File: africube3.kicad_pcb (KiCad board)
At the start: 4 copper layers, 66.5 x 89.5 mm, 41 parts, among them IC1 ADC-20-4, J1 SMA Edge FM, J2 Conn_01x04, J3 RPi_GPIO, J4 Conn_01x02, U1 TQP7M9105, U2 SXBP-150+, U3 BA178M05FP-E2, U4 MCP3421A0T-E/CH

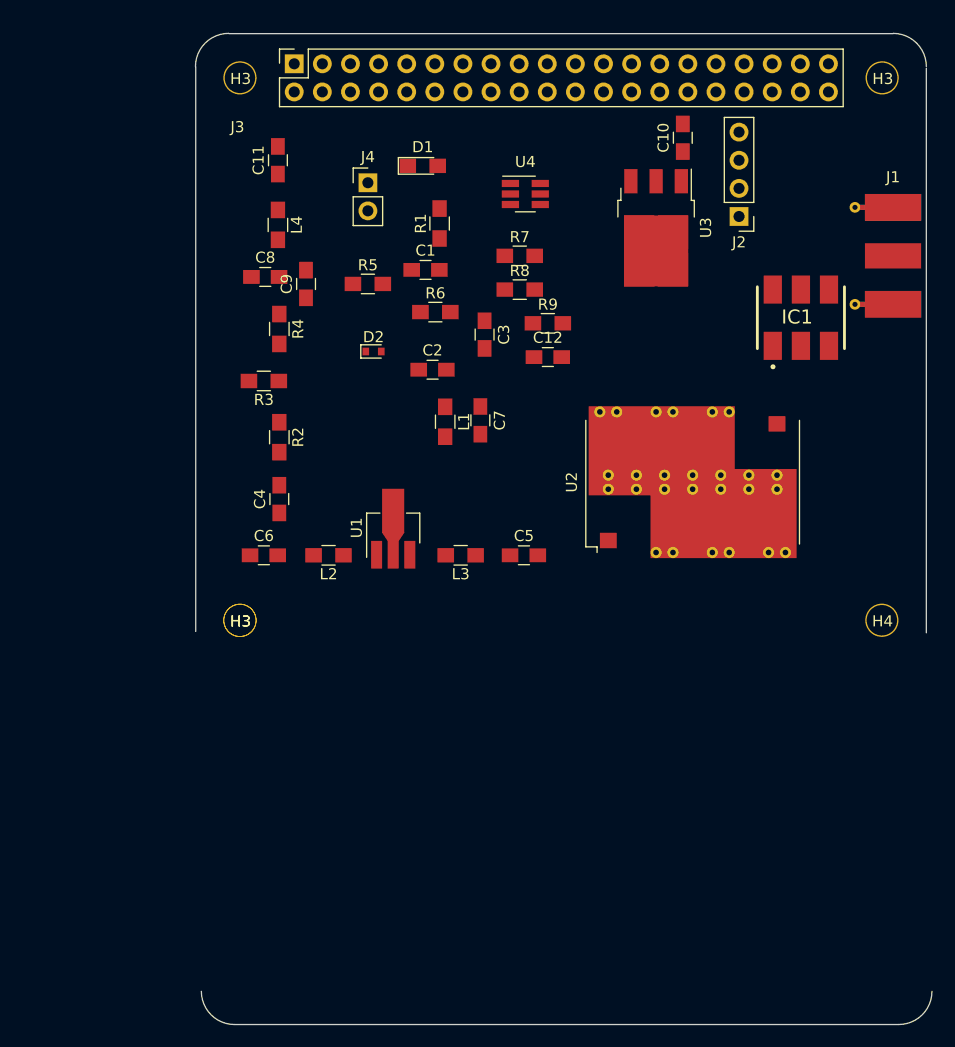
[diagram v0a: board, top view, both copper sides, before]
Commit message: removing power detector
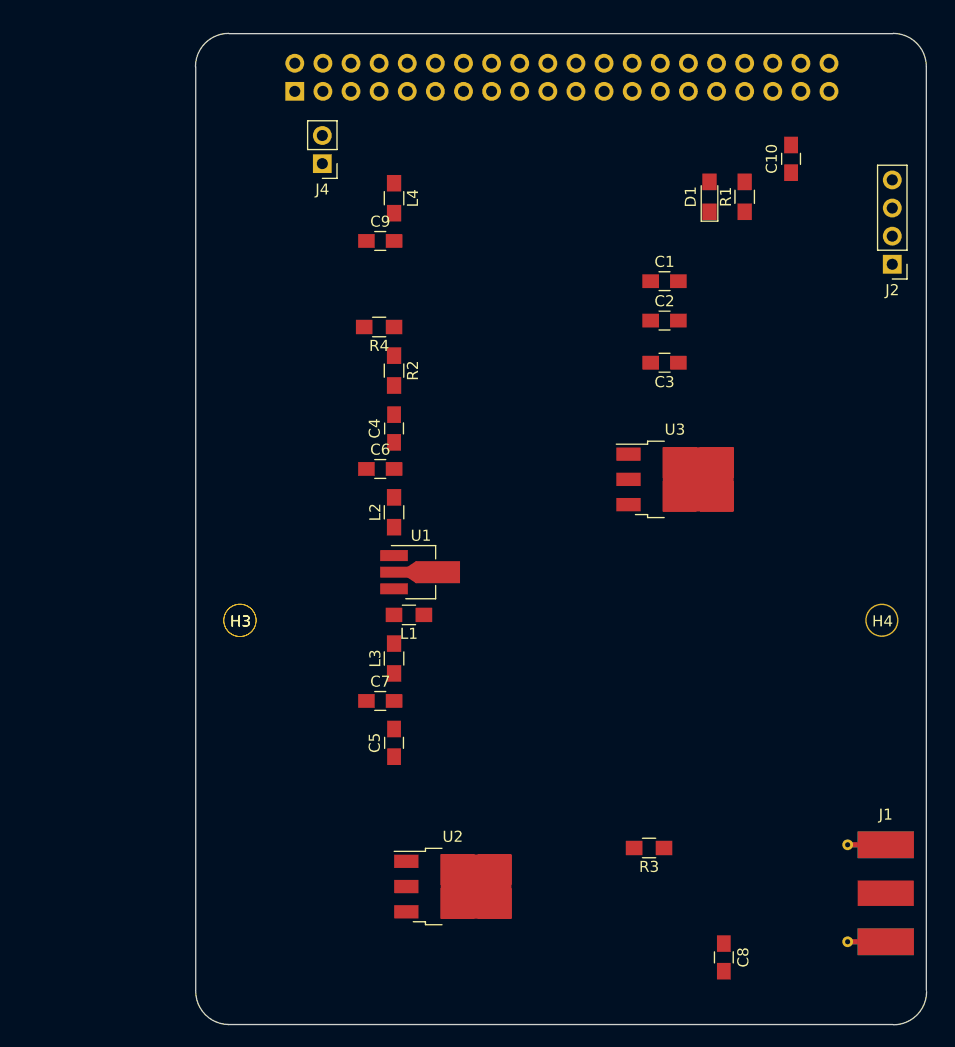
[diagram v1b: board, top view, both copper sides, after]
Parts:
- removed C11: 100pF, Capacitors_SMD:C_0805_HandSoldering
- removed C12: 1nF, Capacitors_SMD:C_0805_HandSoldering
- removed D2: SMS3922-079LF, Diodes_SMD:D_SOD-523
- removed the H3 at (139.0, 64.3)
- removed the H3 at (81.0, 64.3)
- removed IC1: ADC-20-4, rf_noise:ADC-20-4+
- removed R5: 0, Resistors_SMD:R_0805_HandSoldering
- removed R6, R7, R8, R9: 220K, Resistors_SMD:R_0805_HandSoldering
- removed U4: MCP3421A0T-E/CH, TO_SOT_Packages_SMD:SOT-23-6_Handsoldering
- C10: value 4.7uF 16V -> 100pF
- C8: value 100pF -> 10pF
- C9: value 10pF -> 4.7uF 16V
- J3: moved to B.Cu
- R3: value 50 -> OC
- R4: value OC -> 0
- U2: footprint RF_Mini-Circuits:Mini-Circuits_HF1139_LandPatternPL-230 -> TO_SOT_Packages_SMD:TO-252-3_TabPin4
- U3: footprint TO_SOT_Packages_SMD:TO-252-3_TabPin2 -> TO_SOT_Packages_SMD:TO-252-3_TabPin4
- moved C8 74.1 mm to (124.7, 143.8), turned to 270 degrees
- moved J1 57.6 mm to (137.6, 138.0)
- moved R3 54.7 mm to (118.0, 133.9)
- moved U2 42.5 mm to (100.3, 137.4), turned to 0 degrees
- moved R1 27.7 mm to (126.6, 75.1)
- moved C7 26.9 mm to (93.7, 120.6), turned to 0 degrees
- moved D1 26.1 mm to (123.4, 75.1), turned to 90 degrees
- moved U3 22.8 mm to (120.3, 100.6), turned to 0 degrees
- moved C1 21.6 mm to (119.4, 82.7)
- moved C2 21.4 mm to (119.4, 86.2)
- moved C5 20.6 mm to (94.9, 124.4), turned to 90 degrees
- moved L1 17.8 mm to (96.3, 112.8), turned to 180 degrees
- moved C3 16.5 mm to (119.4, 90.0), turned to 180 degrees
- moved J2 14.5 mm to (140.0, 81.2)
- moved C6 13.1 mm to (93.7, 99.6)
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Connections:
- C10 pad 2: GND -> Net-(C10-Pad2)
- C8 pad 1: Net-(C8-Pad1) -> GND
- C9 pad 1: GND -> Net-(C9-Pad1)
- C9 pad 2: Net-(C9-Pad2) -> GND
- J1 pad 1: Net-(IC1-Pad6) -> (no net)
- J2 pad 2: Net-(C10-Pad1) -> Net-(C9-Pad1)
- J3 pad 3: SDA -> (no net)
- J3 pad 5: SCL -> (no net)
- J3 pad 7: Net-(C11-Pad2) -> Net-(C10-Pad2)
- L4 pad 1: Net-(C11-Pad1) -> Net-(C10-Pad1)
- L4 pad 2: Net-(C9-Pad2) -> Net-(C8-Pad2)
- R3 pad 1: Net-(IC1-Pad4) -> Net-(R2-Pad1)
- R4 pad 1: Net-(R2-Pad1) -> Net-(C8-Pad2)
- R4 pad 2: GND -> Net-(R2-Pad1)
- U3 pad 1: Net-(C10-Pad1) -> Net-(C9-Pad1)
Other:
- board size 66.5 x 89.5 mm -> 66.1 x 89.6 mm

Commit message: removed power detection
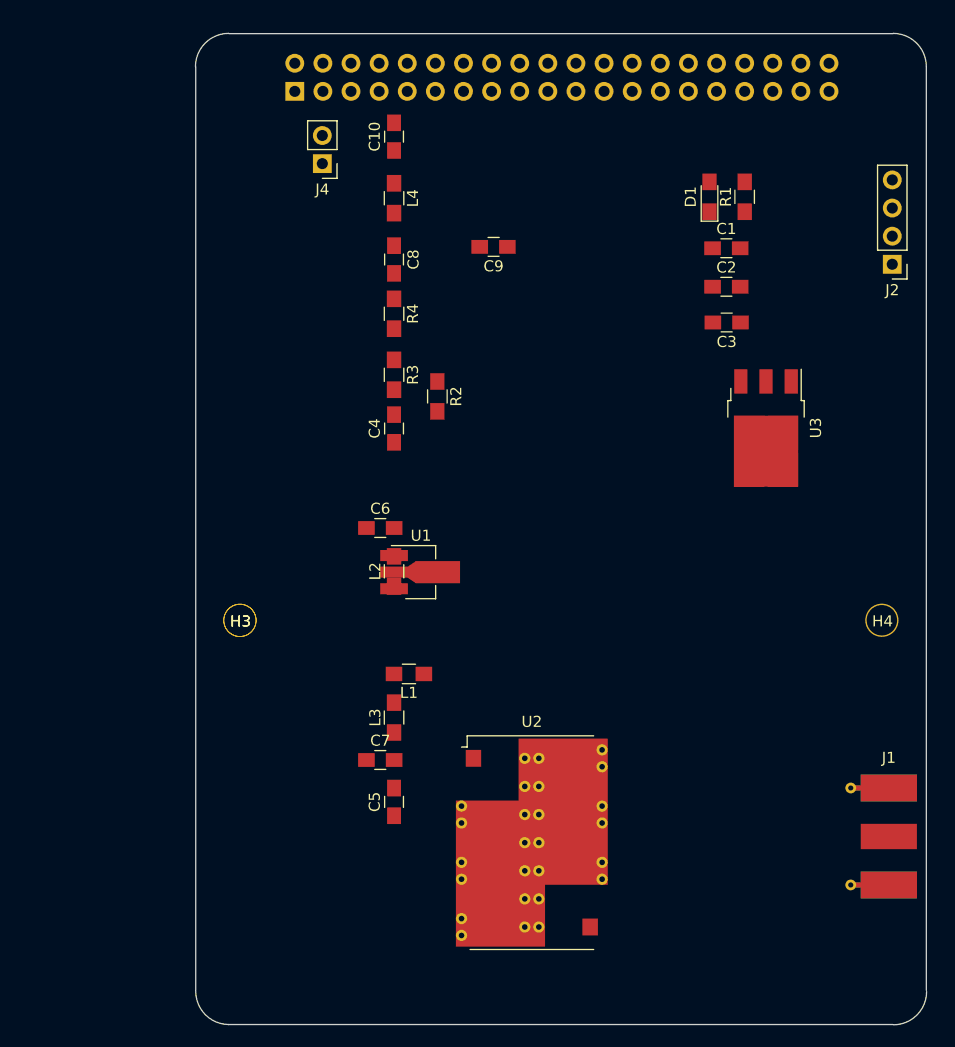
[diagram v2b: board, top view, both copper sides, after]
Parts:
- U2: footprint TO_SOT_Packages_SMD:TO-252-3_TabPin4 -> mini_filter:Mini-Circuits_HF1139_LandPatternPL-230
- moved C8 69.7 mm to (94.9, 80.7)
- moved R3 48.6 mm to (94.9, 91.1), turned to 270 degrees
- moved C10 35.9 mm to (94.9, 69.6)
- moved C9 10.3 mm to (103.9, 79.6), turned to 180 degrees
- moved U3 9.45 mm to (128.5, 95.9), turned to 270 degrees
- moved U2 8.16 mm to (107.4, 133.4)
- moved C3 6.69 mm to (125.0, 86.4)
- moved C2 6.37 mm to (125.0, 83.2)
- moved C1 6.33 mm to (125.0, 79.7)
- moved C5 5.33 mm to (94.9, 129.7)
- moved C6 5.33 mm to (93.7, 105.0)
- moved C7 5.33 mm to (93.7, 125.9)
- moved L3 5.33 mm to (94.9, 122.1)
- moved L1 5.33 mm to (96.3, 118.2)
- moved L2 5.33 mm to (94.9, 108.9)
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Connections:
- J1 pad 1: (no net) -> Net-(J1-Pad1)

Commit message: layout done need to do groundplanes
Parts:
- added H3: 3mm_Mounting_Hole, project_footprints:NPTH_3mm_ID, F.Cu at (81.0, 64.3)
- added H3 (x2): 3mm_Mounting_Hole, project_footprints:NPTH_3mm_ID, F.Cu at (81.6, 114.4)
- added H4: 3mm_Mounting_Hole, project_footprints:NPTH_3mm_ID, F.Cu at (139.0, 64.3)
- added H4: 3mm_Mounting_Hole, project_footprints:NPTH_3mm_ID, F.Cu at (139.0, 113.3)
- moved J4 37.9 mm to (126.3, 70.3), turned to 270 degrees
- moved C9 30.8 mm to (134.7, 79.9), turned to 270 degrees
- moved U2 10.2 mm to (116.3, 138.4), turned to 90 degrees
- moved C5 7.47 mm to (94.9, 137.2)
- moved U1 6.53 mm to (96.9, 115.5)
- moved C7 6.42 mm to (96.2, 131.9), turned to 180 degrees
- moved L3 4.42 mm to (94.9, 126.5)
- moved R2 3.93 mm to (94.9, 93.4)
- moved C4 3.53 mm to (94.9, 99.5)
- moved L1 2.92 mm to (96.3, 121.1)
- moved R3 2.81 mm to (96.3, 88.7), turned to 0 degrees
- moved C6 2.67 mm to (96.2, 104.0), turned to 180 degrees
- moved C8 1.67 mm to (96.2, 79.6), turned to 180 degrees
- moved R4 1.57 mm to (94.9, 84.0)
- moved H3 1.23 mm to (81.6, 114.4)
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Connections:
- J2 pad 4: Net-(J2-Pad4) -> GND
- J3 pad 1: Net-(J2-Pad4) -> (no net)
- J3 pad 17: Net-(J2-Pad4) -> (no net)
- U3 pad 2: (no net) -> GND
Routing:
- net GND: track 0.00 -> 312.9 mm, vias 0 -> 2
- net +5V: track 0.00 -> 92.9 mm
- net Net-(J3-Pad2): track 0.00 -> 70.9 mm
- net Net-(C9-Pad1): track 0.00 -> 20.7 mm
- net Net-(J1-Pad1): track 0.00 -> 16.3 mm
- net Net-(C5-Pad1): track 0.00 -> 16.2 mm
- net Net-(L1-Pad2): track 0.00 -> 8.18 mm
- net Net-(C5-Pad2): track 0.00 -> 8.07 mm
- net Net-(C4-Pad1): track 0.00 -> 6.70 mm
- net Net-(R2-Pad1): track 0.00 -> 6.68 mm
- net Net-(C8-Pad2): track 0.00 -> 6.19 mm
- net Net-(L2-Pad1): track 0.00 -> 3.84 mm
- net Net-(C4-Pad2): track 0.00 -> 3.50 mm
- net Net-(C10-Pad2): track 0.00 -> 3.40 mm
- net Net-(C10-Pad1): track 0.00 -> 2.96 mm
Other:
- copper layers 4 -> 2
- net class 5V2A added: clearance 0.4, trace_width 0.8, via_dia 0.4, via_drill 0.2
- net class Transmition_Line added: clearance 0.2, trace_width 1.05758, via_dia 3, via_drill 1.5

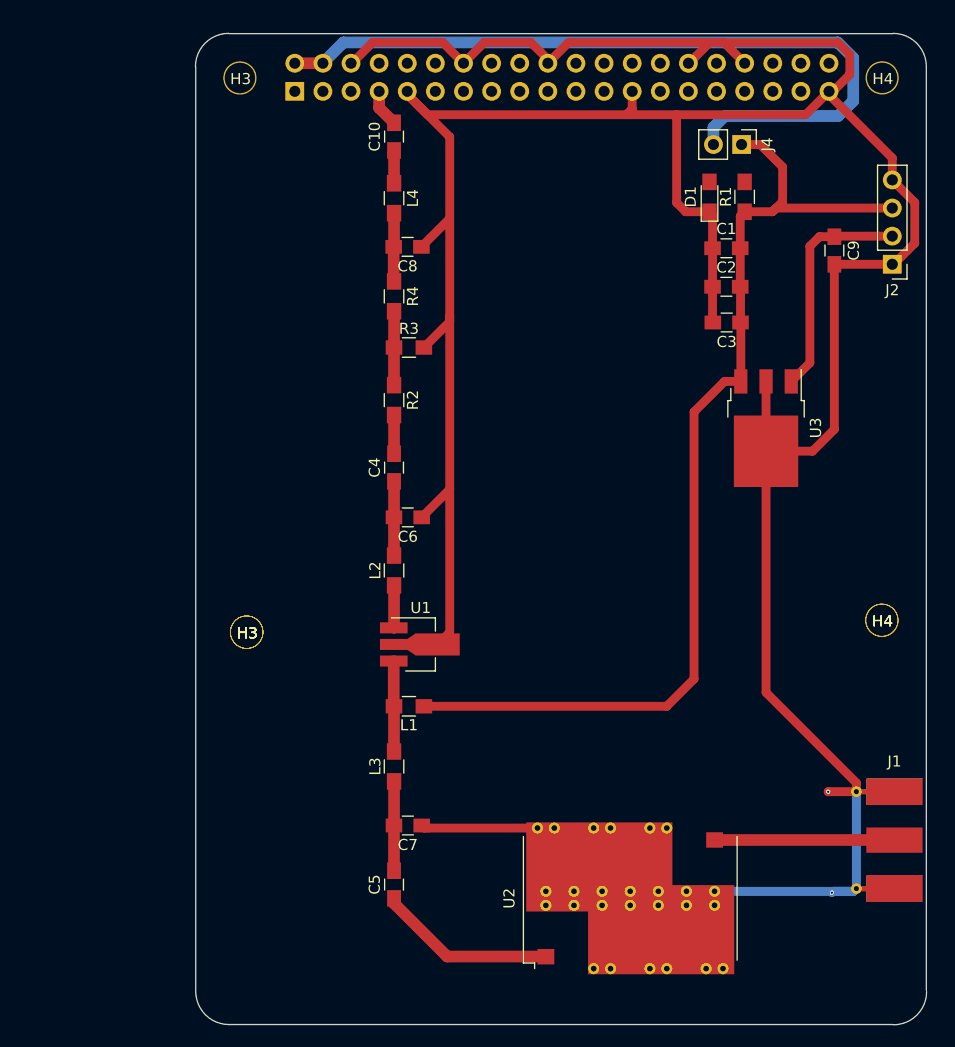
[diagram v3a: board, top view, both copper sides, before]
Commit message: added groundplane
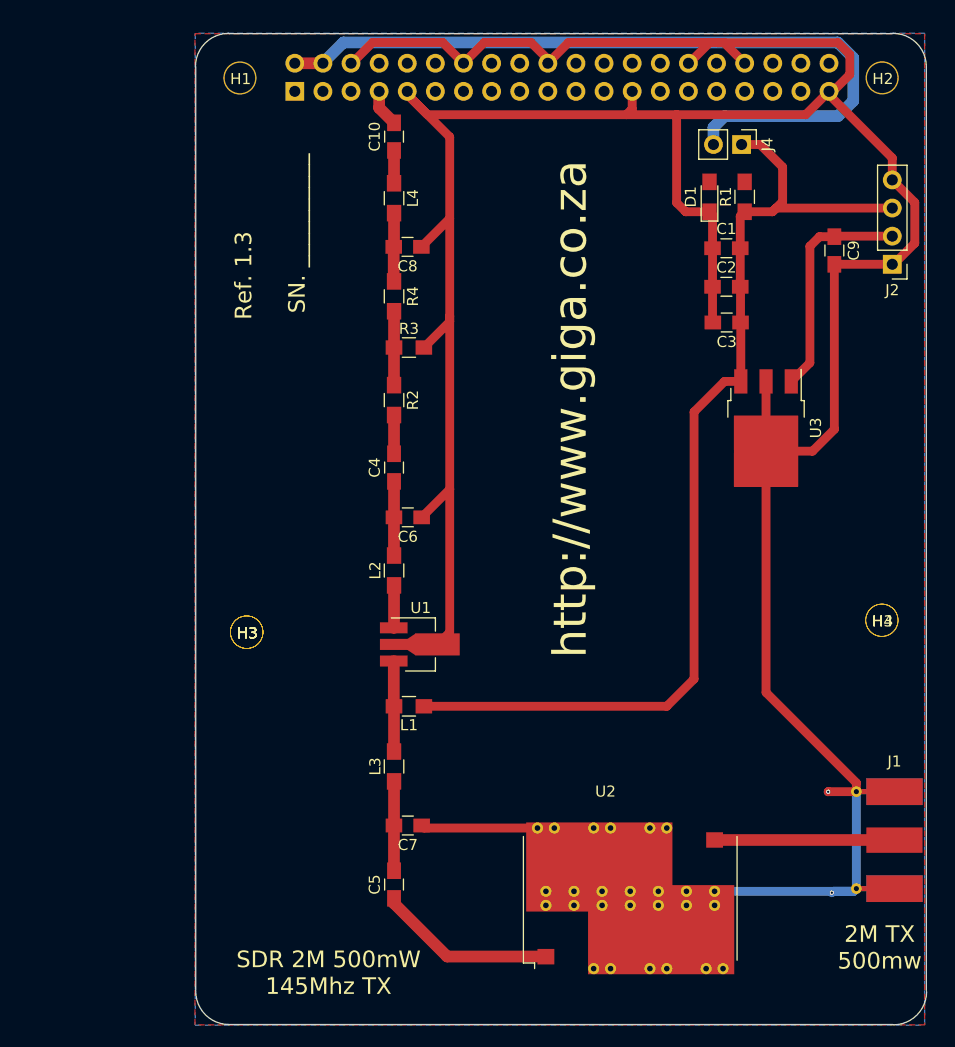
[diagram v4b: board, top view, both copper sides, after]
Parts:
- renumbered H3 to H1, H4 to H2, H4 to H3
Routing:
- added copper zone on B.Cu, net GND
- added copper zone on F.Cu, net GND
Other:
- board text added: "2M TX 500mw"
- board text added: "Ref. 1.3"
- board text added: "SDR 2M 500mW 145Mhz TX"
- board text added: "SN. __________"
- board text added: "http://www.giga.co.za"
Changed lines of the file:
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@@
   (general
     (links 100)
-    (no_connects 8)
-    (area 60.057084 48.379474 153.145001 149.905012)
+    (no_connects 1)
+    (area 76.954955 60.24221 143.105752 149.905012)
     (thickness 1.6)
-    (drawings 18)
+    (drawings 23)
     (tracks 144)
     (zones 0)
@@
     (user_trace_width 2)
     (trace_clearance 0.2)
-    (zone_clearance 0.2)
+    (zone_clearance 0.508)
     (zone_45_only yes)
     (trace_min 0.15)
@@
   )
   (module project_footprints:NPTH_3mm_ID locked (layer F.Cu)
-    (at 139.0394 64.3134)
-    (fp_text reference H4 (at 0.06 0.09) (layer F.SilkS)
+    (at 139.014 113.31)
+    (fp_text reference H3 (at 0.06 0.09) (layer F.SilkS)
       (effects (font (size 1 1) (thickness 0.15)))
     )
@@
   )
   (module project_footprints:NPTH_3mm_ID locked (layer F.Cu)
+    (at 139.0394 64.3134)
+    (fp_text reference H2 (at 0.06 0.09) (layer F.SilkS)
+      (effects (font (size 1 1) (thickness 0.15)))
+    )
+    (fp_text value 3mm_Mounting_Hole (at 0 -2.7) (layer F.Fab)
+      (effects (font (size 1 1) (thickness 0.15)))
+    )
+    (pad "" np_thru_hole circle (at 0 0) (size 3 3) (drill 2.75) (layers *.Cu *.Mask)
+      (clearance 1.6))
+  )
+  (module project_footprints:NPTH_3mm_ID locked (layer F.Cu)
     (at 81.024 64.3234)
-    (fp_text reference H3 (at 0.06 0.09) (layer F.SilkS)
+    (fp_text reference H1 (at 0.06 0.09) (layer F.SilkS)
       (effects (font (size 1 1) (thickness 0.15)))
     )
@@
     (at 81.6336 114.3868)
     (fp_text reference H3 (at 0.06 0.09) (layer F.SilkS)
-      (effects (font (size 1 1) (thickness 0.15)))
-    )
-    (fp_text value 3mm_Mounting_Hole (at 0 -2.7) (layer F.Fab)
-      (effects (font (size 1 1) (thickness 0.15)))
-    )
-    (pad "" np_thru_hole circle (at 0 0) (size 3 3) (drill 2.75) (layers *.Cu *.Mask)
-      (clearance 1.6))
-  )
-  (module project_footprints:NPTH_3mm_ID locked (layer F.Cu)
-    (at 139.014 113.31)
-    (fp_text reference H4 (at 0.06 0.09) (layer F.SilkS)
       (effects (font (size 1 1) (thickness 0.15)))
     )
@@
     (tags "Mini-Circuits PL-230")
     (attr smd)
-    (fp_text reference U2 (at 0 -10.922 90) (layer F.SilkS)
+    (fp_text reference U2 (at 9.652 -2.2352 180) (layer F.SilkS)
       (effects (font (size 1 1) (thickness 0.15)))
     )
@@
     )
   )
+  (gr_text "SDR 2M 500mW\n145Mhz TX" (at 89.027 145.161) (layer F.SilkS)
+    (effects (font (size 1.5 1.5) (thickness 0.3)))
+  )
+  (gr_text "2M TX\n500mw" (at 138.811 142.875) (layer F.SilkS)
+    (effects (font (size 1.5 1.5) (thickness 0.3)))
+  )
+  (gr_text "SN. __________" (at 86.1822 78.359 90) (layer F.SilkS)
+    (effects (font (size 1.5 1.5) (thickness 0.3)))
+  )
+  (gr_text "Ref. 1.3" (at 81.3562 82.169 90) (layer F.SilkS)
+    (effects (font (size 1.5 1.5) (thickness 0.3)))
+  )
+  (gr_text http://www.giga.co.za (at 110.871 94.234 90) (layer F.SilkS)
+    (effects (font (size 3 3) (thickness 0.3)))
+  )
+  (gr_circle (center 139.030356 113.317611) (end 140.405356 113.317611) (layer Dwgs.User) (width 0.1))
   (gr_circle (center 81.639956 114.384411) (end 83.014956 114.384411) (layer Dwgs.User) (width 0.1))
   (gr_circle (center 81.639956 114.384411) (end 83.014956 114.384411) (layer Dwgs.User) (width 0.1))
@@
   (gr_arc (start 140.030356 63.292211) (end 143.030356 63.292211) (angle -90) (layer Edge.Cuts) (width 0.1))
   (gr_line (start 143.030356 63.3176) (end 143.030356 146.75) (layer Edge.Cuts) (width 0.1))
-  (gr_circle (center 139.030356 113.317611) (end 140.405356 113.317611) (layer Dwgs.User) (width 0.1))
   (gr_circle (center 139.030356 64.317611) (end 140.405356 64.317611) (layer Dwgs.User) (width 0.1))
   (gr_circle (center 81.030356 64.317611) (end 82.405356 64.317611) (layer Dwgs.User) (width 0.1))
@@
   (segment (start 123.9012 133.1595) (end 140.1373 133.1595) (width 1.05758) (layer F.Cu) (net 16))
   (segment (start 140.1373 133.1595) (end 140.15 133.1722) (width 1.05758) (layer F.Cu) (net 16))
+  (zone (net 1) (net_name GND) (layer F.Cu) (hatch edge 0.508)
+    (connect_pads (clearance 0.508))
+    (min_thickness 0.254)
+    (fill yes (arc_segments 16) (thermal_gap 0.508) (thermal_bridge_width 0.508))
+    (polygon
+      (pts
+        (xy 142.875 149.86) (xy 76.962 149.86) (xy 76.962 60.325) (xy 142.875 60.325)
+      )
+    )
+  )
+  (zone (net 1) (net_name GND) (layer B.Cu) (hatch edge 0.508)
+    (connect_pads (clearance 0.508))
+    (min_thickness 0.254)
+    (fill yes (arc_segments 16) (thermal_gap 0.508) (thermal_bridge_width 0.508))
+    (polygon
+      (pts
+        (xy 76.9874 60.2742) (xy 76.9874 149.8854) (xy 142.875 149.8854) (xy 142.875 60.2742)
+      )
+    )
+  )
 )

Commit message: Created gerber files
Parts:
- moved C1 46.2 mm to (107.1, 122.3), turned to 90 degrees
- moved C2 41.6 mm to (110.7, 122.3), turned to 90 degrees
- moved J1 5.72 mm to (137.7, 127.5)
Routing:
- net GND: track 312.9 -> 257.7 mm, vias 2 -> 61
- net Net-(C5-Pad1): track 16.2 -> 24.9 mm
- net Net-(J1-Pad1): track 16.3 -> 19.8 mm

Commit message: upgrade modules to new cad
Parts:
- added REF**: Socket_Strip_Straight_2x20_Pitch2.54mm, pc104:Socket_Strip_Straight_2x20_Pitch2.54mm, B.Cu at (86.0, 65.5)
